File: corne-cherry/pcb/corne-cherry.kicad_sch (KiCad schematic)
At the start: 124 parts, among them J2 OLED, J3 MJ-4PP-9, J4 OLED, SW1 SW_PUSH, SW10 SW_PUSH, SW11 SW_PUSH, SW12 SW_PUSH, SW13 SW_PUSH, SW14 SW_PUSH, SW15 SW_PUSH, SW16 SW_PUSH, SW17 SW_PUSH, SW18 SW_PUSH, SW19 SW_PUSH, SW2 SW_PUSH, SW20 SW_PUSH, SW21 SW_PUSH, SW22 SW_PUSH, SW23 SW_PUSH, SW24 SW_PUSH, SW25 SW_PUSH, SW26 SW_PUSH, SW27 SW_PUSH, SW28 SW_PUSH, SW29 SW_PUSH, SW3 SW_PUSH, SW30 SW_PUSH, SW31 SW_PUSH, SW32 SW_PUSH, SW33 SW_PUSH, SW34 SW_PUSH, SW35 SW_PUSH, SW36 SW_PUSH, SW37 SW_PUSH, SW38 SW_PUSH, SW39 SW_PUSH, SW4 SW_PUSH, SW40 SW_PUSH, SW41 SW_PUSH, SW42 SW_PUSH, SW5 SW_PUSH, SW6 SW_PUSH, SW7 SW_PUSH, SW8 SW_PUSH, SW9 SW_PUSH, U1 ProMicro, U2 ProMicro

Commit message: finished all traces
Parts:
- removed J3: MJ-4PP-9, kbd:MJ-4PP-9_1side, symbol kbd:MJ-4PP-9
- removed LED28, LED29, LED30, LED31, LED32, LED33: WS2812B, LED_SMD:LED_WS2812B_PLCC4_5.0x5.0mm_P3.2mm, symbol LED:WS2812B
- removed LED34, LED35, LED36, LED37, LED38, LED39, LED40, LED41, LED42, LED43, LED44, LED45, LED46, LED47, LED48, LED49, LED50, LED51, LED52, LED53, LED54: YS-SK6812MINI-E, kbd:YS-SK6812MINI-E, symbol kbd:YS-SK6812MINI-E
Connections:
- no-connect marks 10 -> 8

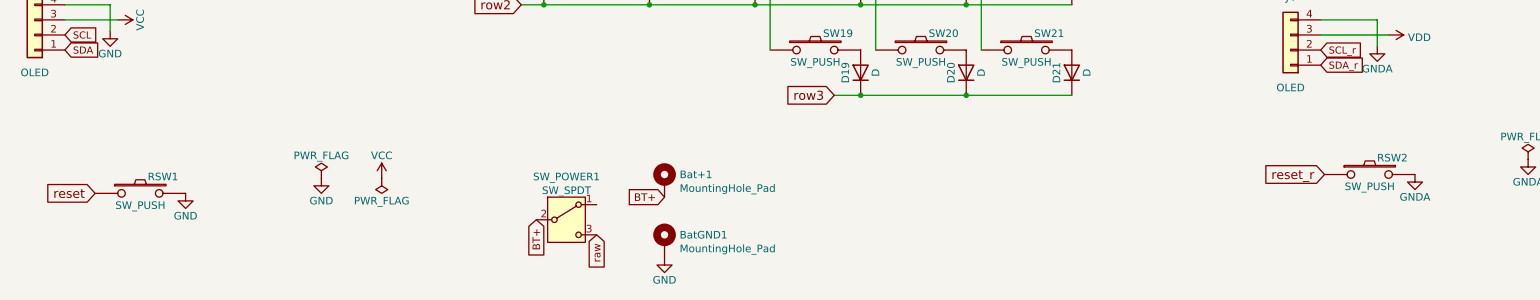
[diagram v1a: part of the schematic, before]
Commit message: removed reset button
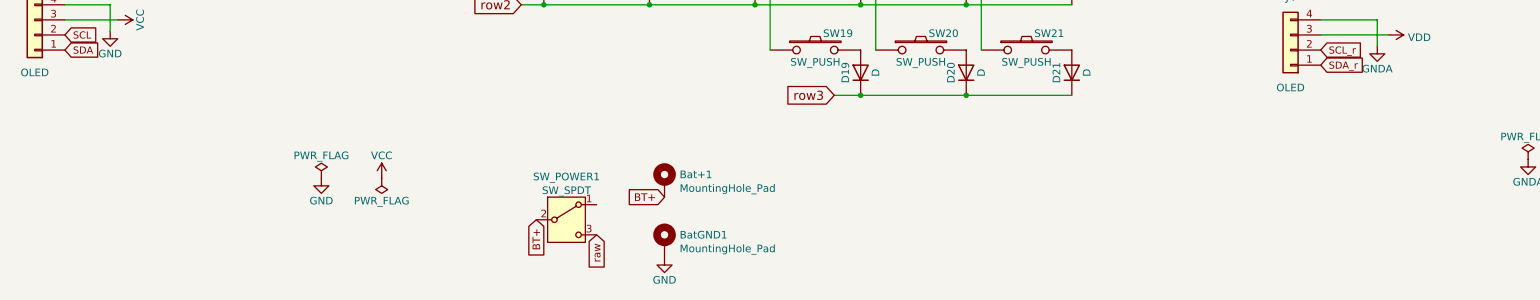
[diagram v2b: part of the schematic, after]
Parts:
- removed RSW1, RSW2: SW_PUSH, kbd:ResetSW_1side, symbol kbd:SW_PUSH
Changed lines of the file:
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@@
-    )
-  )
-  (global_label "reset" (shape input) (at 31.115 102.235 180) (fields_autoplaced)
-    (effects (font (size 1.524 1.524)) (justify right))
-    (property "Intersheetrefs" "${INTERSHEET_REFS}" (at 22.6576 102.235 0)
-      (effects (font (size 1.27 1.27)) (justify right) hide)
     )
   )
@@
     (effects (font (size 1.1938 1.1938)) (justify right))
     (property "Intersheetrefs" "${INTERSHEET_REFS}" (at 21.8169 42.545 0)
-      (effects (font (size 1.27 1.27)) (justify right) hide)
-    )
-  )
-  (global_label "reset_r" (shape input) (at 238.125 99.06 180) (fields_autoplaced)
-    (effects (font (size 1.524 1.524)) (justify right))
-    (property "Intersheetrefs" "${INTERSHEET_REFS}" (at 227.5631 99.06 0)
       (effects (font (size 1.27 1.27)) (justify right) hide)
     )
@@
     )
   )
-  (symbol (lib_id "kbd:SW_PUSH") (at 38.735 102.235 0) (unit 1)
-    (in_bom yes) (on_board yes) (dnp no)
-    (property "Reference" "RSW1" (at 42.545 99.441 0)
-      (effects (font (size 1.27 1.27)))
-    )
-    (property "Value" "SW_PUSH" (at 38.735 104.267 0)
-      (effects (font (size 1.27 1.27)))
-    )
-    (property "Footprint" "kbd:ResetSW_1side" (at 38.735 102.235 0)
-      (effects (font (size 1.27 1.27)) hide)
-    )
-    (property "Datasheet" "" (at 38.735 102.235 0)
-      (effects (font (size 1.27 1.27)))
-    )
-    (pin "1")
-    (pin "2")
-    (instances
-      (project "corne-cherry"
-        (path "/4cc5d416-57f5-4147-8183-e03ae6b1198a"
-          (reference "RSW1") (unit 1)
-        )
-      )
-    )
-  )
-  (symbol (lib_id "power:GND") (at 46.355 102.235 0) (unit 1)
-    (in_bom yes) (on_board yes) (dnp no)
-    (property "Reference" "#PWR06" (at 46.355 108.585 0)
-      (effects (font (size 1.27 1.27)) hide)
-    )
-    (property "Value" "GND" (at 46.355 106.045 0)
-      (effects (font (size 1.27 1.27)))
-    )
-    (property "Footprint" "" (at 46.355 102.235 0)
-      (effects (font (size 1.27 1.27)) hide)
-    )
-    (property "Datasheet" "" (at 46.355 102.235 0)
-      (effects (font (size 1.27 1.27)) hide)
-    )
-    (pin "1")
-    (instances
-      (project "corne-cherry"
-        (path "/4cc5d416-57f5-4147-8183-e03ae6b1198a"
-          (reference "#PWR06") (unit 1)
-        )
-      )
-    )
-  )
   (symbol (lib_id "Connector_Generic:Conn_01x04") (at 20.955 75.565 180) (unit 1)
     (in_bom yes) (on_board yes) (dnp no)
@@
         )
       )
-    )
-  )
-  (symbol (lib_id "kbd:SW_PUSH") (at 245.745 99.06 0) (unit 1)
-    (in_bom yes) (on_board yes) (dnp no)
-    (property "Reference" "RSW2" (at 249.555 96.266 0)
-      (effects (font (size 1.27 1.27)))
-    )
-    (property "Value" "SW_PUSH" (at 245.745 101.092 0)
-      (effects (font (size 1.27 1.27)))
-    )
-    (property "Footprint" "kbd:ResetSW_1side" (at 245.745 99.06 0)
-      (effects (font (size 1.27 1.27)) hide)
-    )
-    (property "Datasheet" "" (at 245.745 99.06 0)
-      (effects (font (size 1.27 1.27)))
-    )
-    (pin "1")
-    (pin "2")
-    (instances
-      (project "corne-cherry"
-        (path "/4cc5d416-57f5-4147-8183-e03ae6b1198a"
-          (reference "RSW2") (unit 1)
-        )
-      )
-    )
-  )
-  (symbol (lib_id "power:GNDA") (at 253.365 99.06 0) (unit 1)
-    (in_bom yes) (on_board yes) (dnp no)
-    (property "Reference" "#PWR020" (at 253.365 105.41 0)
-      (effects (font (size 1.27 1.27)) hide)
-    )
-    (property "Value" "GNDA" (at 253.365 102.87 0)
-      (effects (font (size 1.27 1.27)))
-    )
-    (property "Footprint" "" (at 253.365 99.06 0)
-      (effects (font (size 1.27 1.27)) hide)
-    )
-    (property "Datasheet" "" (at 253.365 99.06 0)
-      (effects (font (size 1.27 1.27)) hide)
-    )
-    (pin "1")
-    (instances
-      (project "corne-cherry"
-        (path "/4cc5d416-57f5-4147-8183-e03ae6b1198a"
-          (reference "#PWR020") (unit 1)
-        )
-      )
